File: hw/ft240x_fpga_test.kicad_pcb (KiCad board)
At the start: 4 copper layers, 100 x 60 mm, 253 parts, among them J1 Ext_Power, J10 BNC, J11 PEN_SEL, J12 PUDC_B/IN, J2 USB_C_Receptacle_USB2.0, J3 Jtag_Master, J4 JTAG, J5 GPIO2V5, J6 BNC, J7 BNC, J8 BNC, J9 Expansion, Q1 Si3477, Q2 Si3477, SW1 PROG_B, U1 TLV62569DDC, U10 LMH6882, U11 TSV992A, U12 OPA859xDSG, U13 OPA859xDSG, U14 MCP47CVB02-E_UN, U15 UTC2000, U16 74LVC1G32, U17 SN74LVC2T45DCUR, U2 TLV62569DDC, U3 TLV62569DDC, U4 FT240XS, U5 XC3S50A-VQ100, U6 AT25DF041B, U7 5P49V5925, U8 THS4522, U9 MAX19507, Y1 25MHz

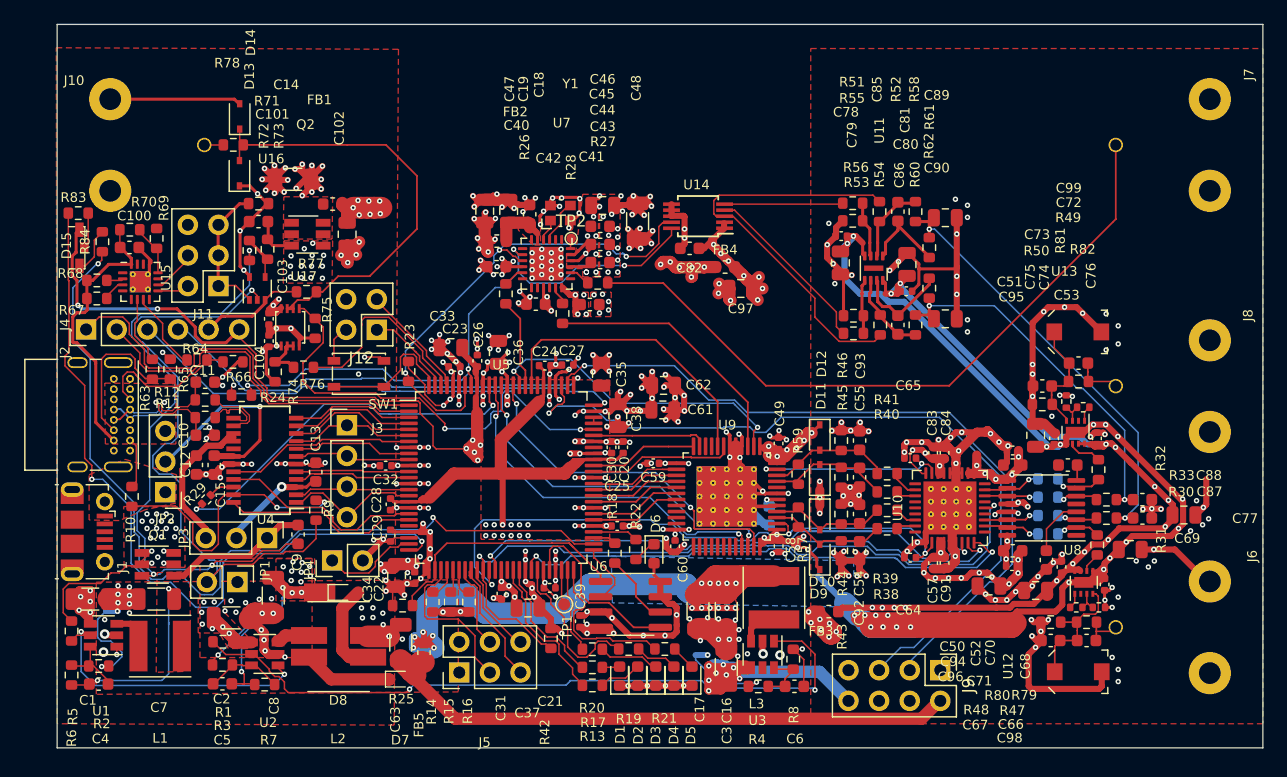
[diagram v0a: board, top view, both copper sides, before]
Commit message: updated gerber options according to jlcpcb instructions
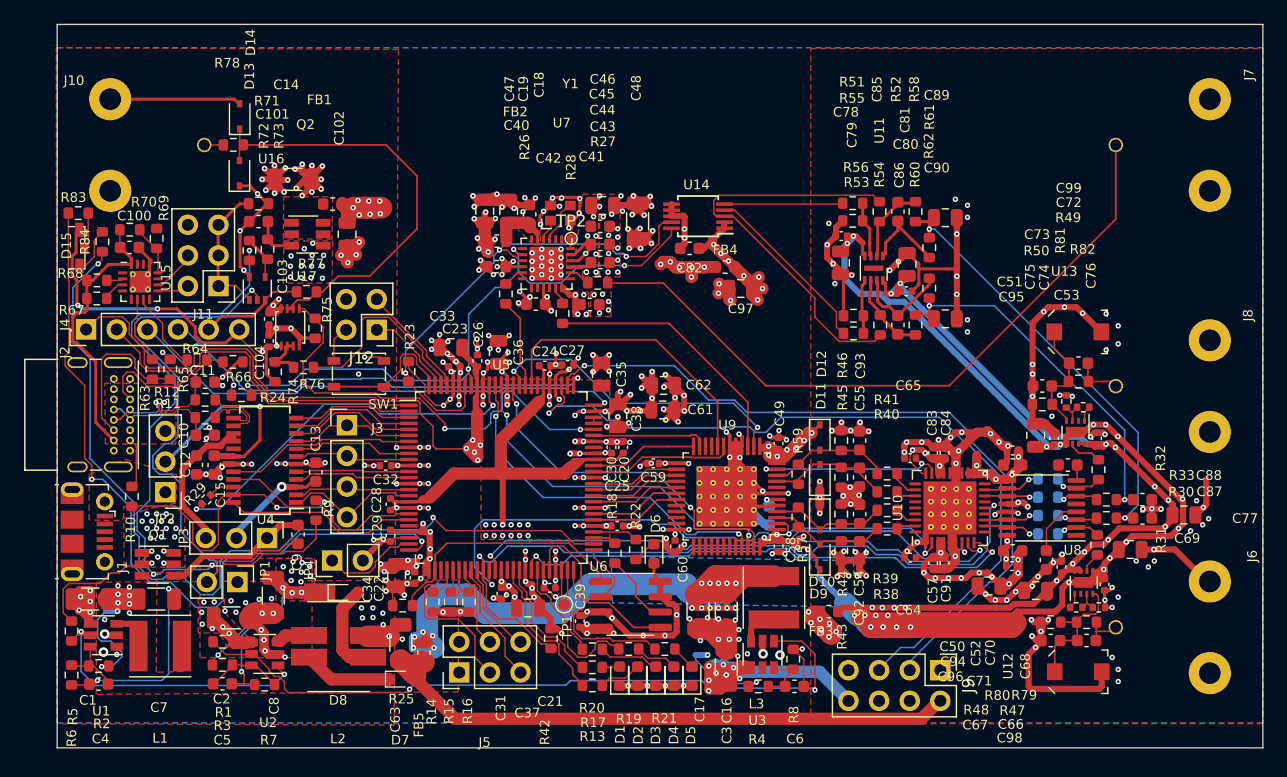
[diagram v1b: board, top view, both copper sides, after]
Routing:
- added copper zone on B.Cu, net GND
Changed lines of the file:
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@@
   )
   (zone (net 139) (net_name -2V5) (layer B.Cu) (hatch edge 0.508)
+    (priority 1)
     (connect_pads yes (clearance 0))
     (min_thickness 0.254)
@@
     (connect_pads (clearance 0))
     (min_thickness 0.127)
-    (fill yes (arc_segments 32) (thermal_gap 0.508) (thermal_bridge_width 0.508))
+    (fill yes (arc_segments 32) (thermal_gap 0.3) (thermal_bridge_width 0.508))
     (polygon
       (pts
@@
       )
     )
+  )
+  (zone (net 1) (net_name GND) (layer B.Cu) (hatch edge 0.508)
+    (connect_pads thru_hole_only (clearance 0))
+    (min_thickness 0.127)
+    (fill yes (arc_segments 32) (thermal_gap 0.3) (thermal_bridge_width 0.508))
+    (polygon
+      (pts
+        (xy 163 80.94) (xy 63 80.94) (xy 63 24.94) (xy 163 24.94)
+      )
+    )
